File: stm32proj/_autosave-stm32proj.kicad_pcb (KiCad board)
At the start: 2 copper layers, 24.1 x 21.6 mm, 29 parts, among them J1 Conn_01x04_Pin, J2 Conn_01x04_Pin, J3 USB_C_Receptacle_USB2.0_14P, U1 STM32F103C8Tx, U2 AMS1117-3.3, U3 AS5600, Y1 8MHz

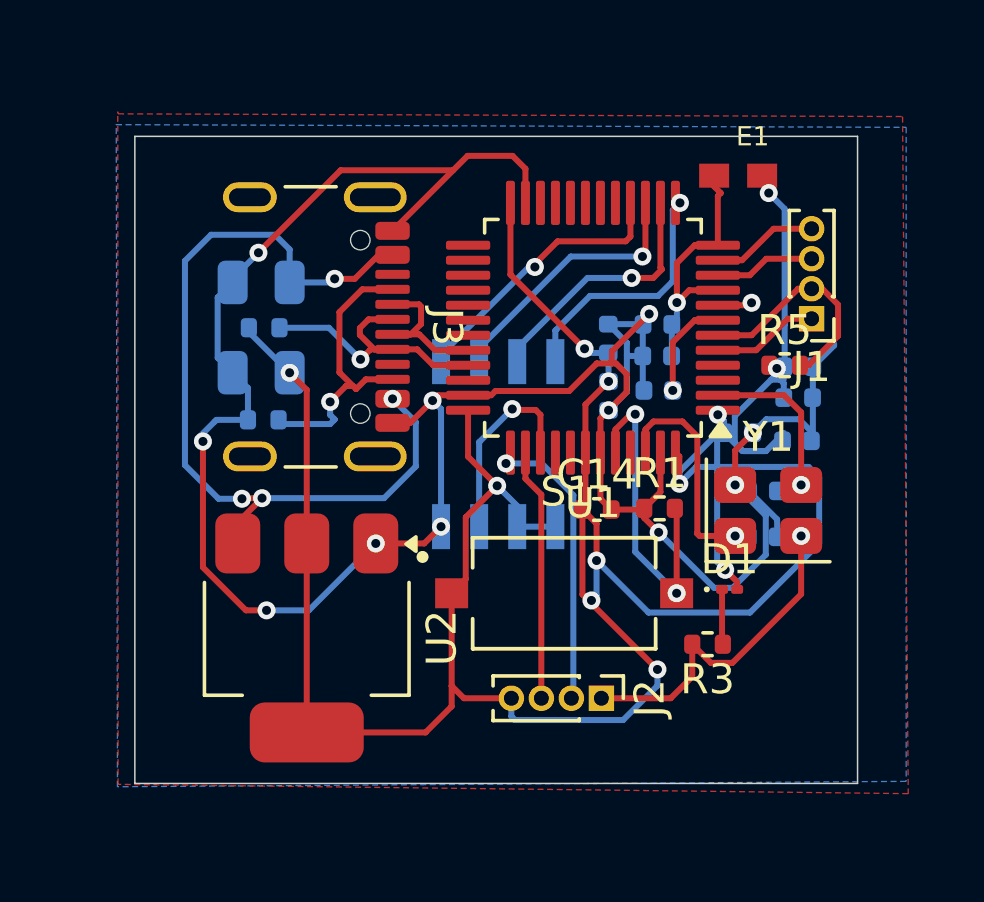
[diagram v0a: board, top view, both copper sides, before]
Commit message: connection errors resolved
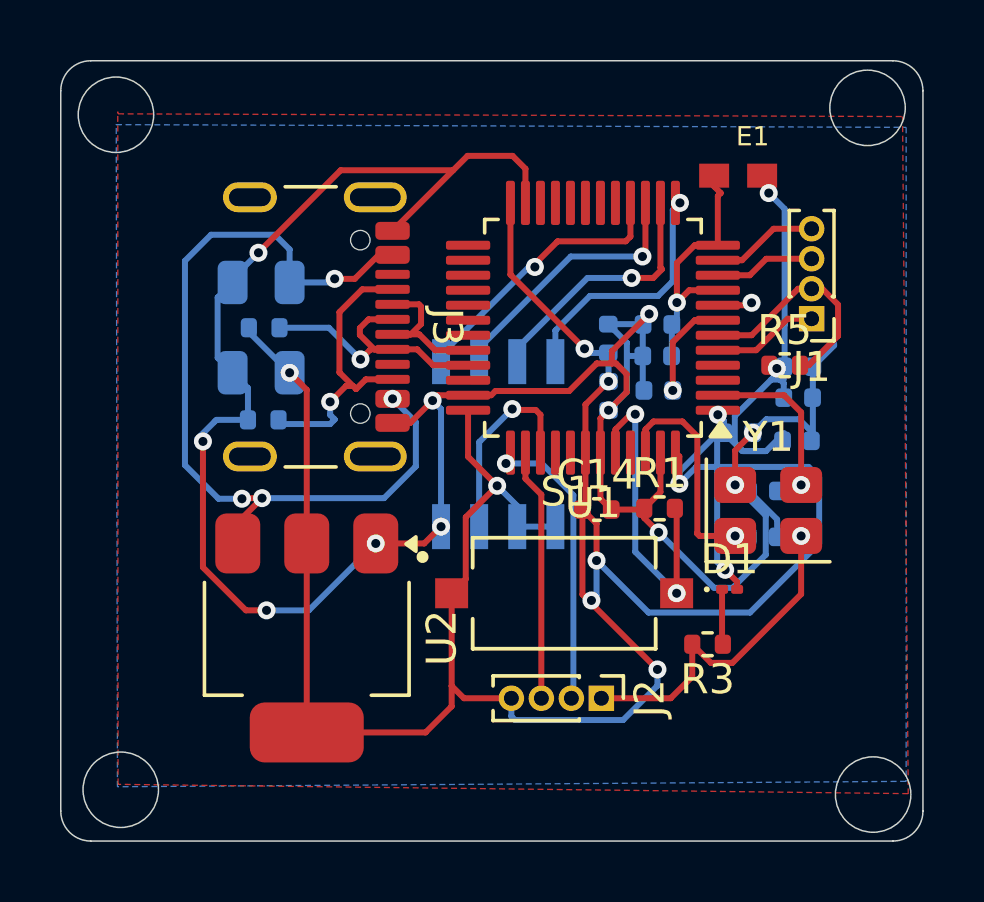
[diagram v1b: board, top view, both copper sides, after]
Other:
- board size 24.1 x 21.6 mm -> 28.7 x 26 mm
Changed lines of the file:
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@@
 		)
 	)
-	(gr_rect
-		(start 112.34 58.29)
-		(end 136.43 79.86)
+	(gr_circle
+		(center 111.71 57.57)
+		(end 112.3 58.68)
 		(stroke
 			(width 0.05)
+			(type default)
+		)
+		(fill no)
+		(layer "Edge.Cuts")
+	)
+	(gr_line
+		(start 109.87 80.78)
+		(end 109.87 56.77)
+		(stroke
+			(width 0.05)
+			(type default)
+		)
+		(layer "Edge.Cuts")
+	)
+	(gr_arc
+		(start 110.87 81.78)
+		(mid 110.162893 81.487107)
+		(end 109.87 80.78)
+		(stroke
+			(width 0.05)
+			(type default)
+		)
+		(layer "Edge.Cuts")
+	)
+	(gr_arc
+		(start 137.61 55.77)
+		(mid 138.317107 56.062893)
+		(end 138.61 56.77)
+		(stroke
+			(width 0.05)
+			(type default)
+		)
+		(layer "Edge.Cuts")
+	)
+	(gr_line
+		(start 110.87 55.77)
+		(end 137.61 55.77)
+		(stroke
+			(width 0.05)
+			(type default)
+		)
+		(layer "Edge.Cuts")
+	)
+	(gr_arc
+		(start 109.87 56.77)
+		(mid 110.162893 56.062893)
+		(end 110.87 55.77)
+		(stroke
+			(width 0.05)
+			(type default)
+		)
+		(layer "Edge.Cuts")
+	)
+	(gr_circle
+		(center 111.87 80.07)
+		(end 112.46 81.18)
+		(stroke
+			(width 0.05)
+			(type default)
+		)
+		(fill no)
+		(layer "Edge.Cuts")
+	)
+	(gr_line
+		(start 137.61 81.78)
+		(end 110.87 81.78)
+		(stroke
+			(width 0.05)
+			(type default)
+		)
+		(layer "Edge.Cuts")
+	)
+	(gr_line
+		(start 138.61 56.77)
+		(end 138.61 80.78)
+		(stroke
+			(width 0.05)
+			(type default)
+		)
+		(layer "Edge.Cuts")
+	)
+	(gr_circle
+		(center 136.95 80.23)
+		(end 137.54 81.34)
+		(stroke
+			(width 0.05)
+			(type default)
+		)
+		(fill no)
+		(layer "Edge.Cuts")
+	)
+	(gr_arc
+		(start 138.61 80.78)
+		(mid 138.317107 81.487107)
+		(end 137.61 81.78)
+		(stroke
+			(width 0.05)
+			(type default)
+		)
+		(layer "Edge.Cuts")
+	)
+	(gr_circle
+		(center 136.76294 57.34)
+		(end 137.35294 58.45)
+		(stroke
+			(width 0.05)
